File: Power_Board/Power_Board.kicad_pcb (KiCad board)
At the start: 2 copper layers, 3 parts, among them J1 Conn_01x10, J2 Conn_01x10, J3 Conn_01x10_Female

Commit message: few things added
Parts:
- removed J2: Conn_01x10, Connector_PinHeader_2.00mm:PinHeader_1x10_P2.00mm_Vertical
- removed J3: Conn_01x10_Female, Connector_PinSocket_1.00mm:PinSocket_1x10_P1.00mm_Vertical
- added J1_left1: Conn_01x12_Female, Connector_PinSocket_2.54mm:PinSocket_1x12_P2.54mm_Vertical, F.Cu at (187.9, 65.2)
- added J1_right1: Conn_01x12_Female, Connector_PinSocket_2.54mm:PinSocket_1x12_P2.54mm_Vertical, F.Cu at (172.7, 65.2)
- added R1: R, Resistor_SMD:R_0201_0603Metric, F.Cu at (157.8, 60.0)
- J1: value Conn_01x10 -> Screw_Terminal_01x02; footprint Connector_PinHeader_2.00mm:PinHeader_1x10_P2.00mm_Vertical -> TerminalBlock_RND:TerminalBlock_RND_205-00001_1x02_P5.00mm_Horizontal
- moved J1 52.4 mm to (199.6, 54.8)
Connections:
- J1 pad 1: unconnected-(J1-Pad1) -> GND
- J1 pad 2: unconnected-(J1-Pad2) -> +BATT
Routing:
- net VBUS: track 0.00 -> 19.4 mm
- net unconnected-(J1_right1-Pad2): track 0.00 -> 17.9 mm

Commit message: LED added for git test
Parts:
- added D1: LED, LED_THT:LED_D5.0mm, F.Cu at (213.4, 66.0)
- added D2: LED, LED_THT:LED_D5.0mm, F.Cu at (213.4, 76.2)
- added R1: R, OptoDevice:R_LDR_5.2x5.2mm_P3.5mm_Horizontal, F.Cu at (220.0, 66.0)
- added R2: R, OptoDevice:R_LDR_5.2x5.2mm_P3.5mm_Horizontal, F.Cu at (220.0, 76.2)

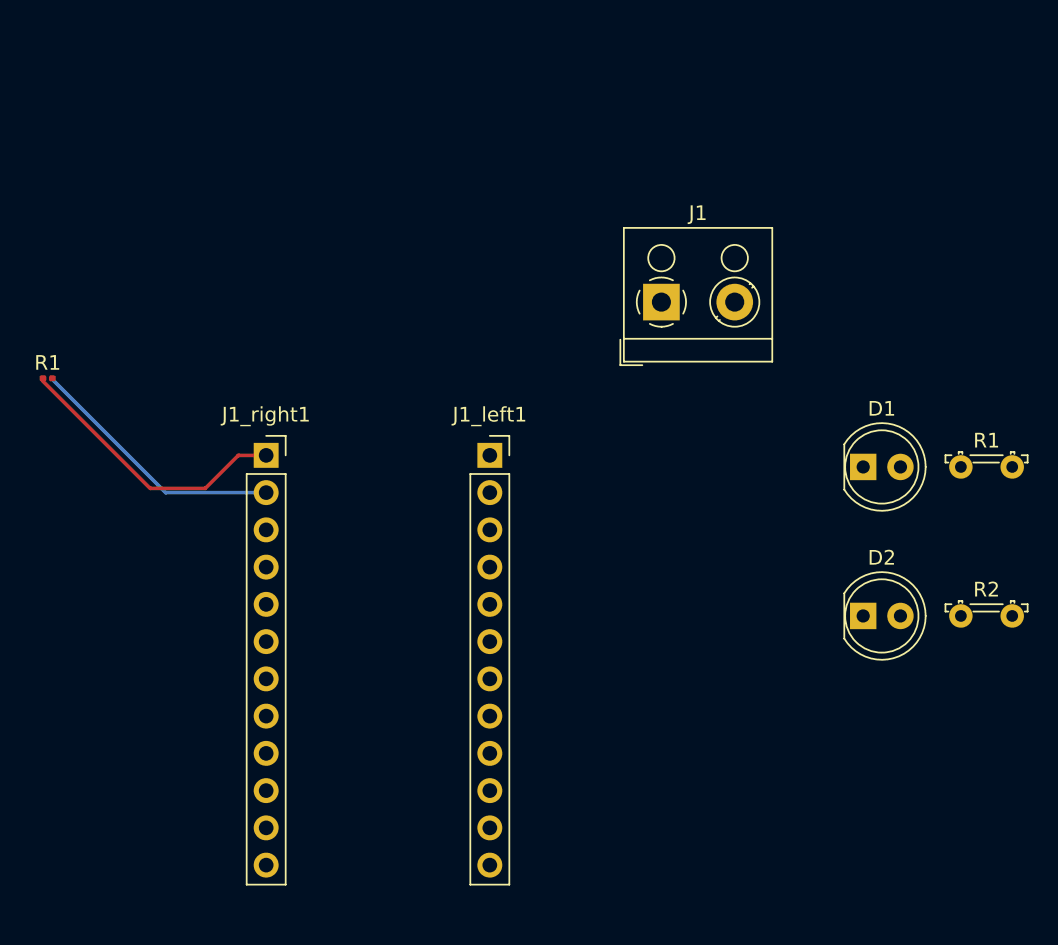
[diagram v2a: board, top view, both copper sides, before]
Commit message: sensor adeed
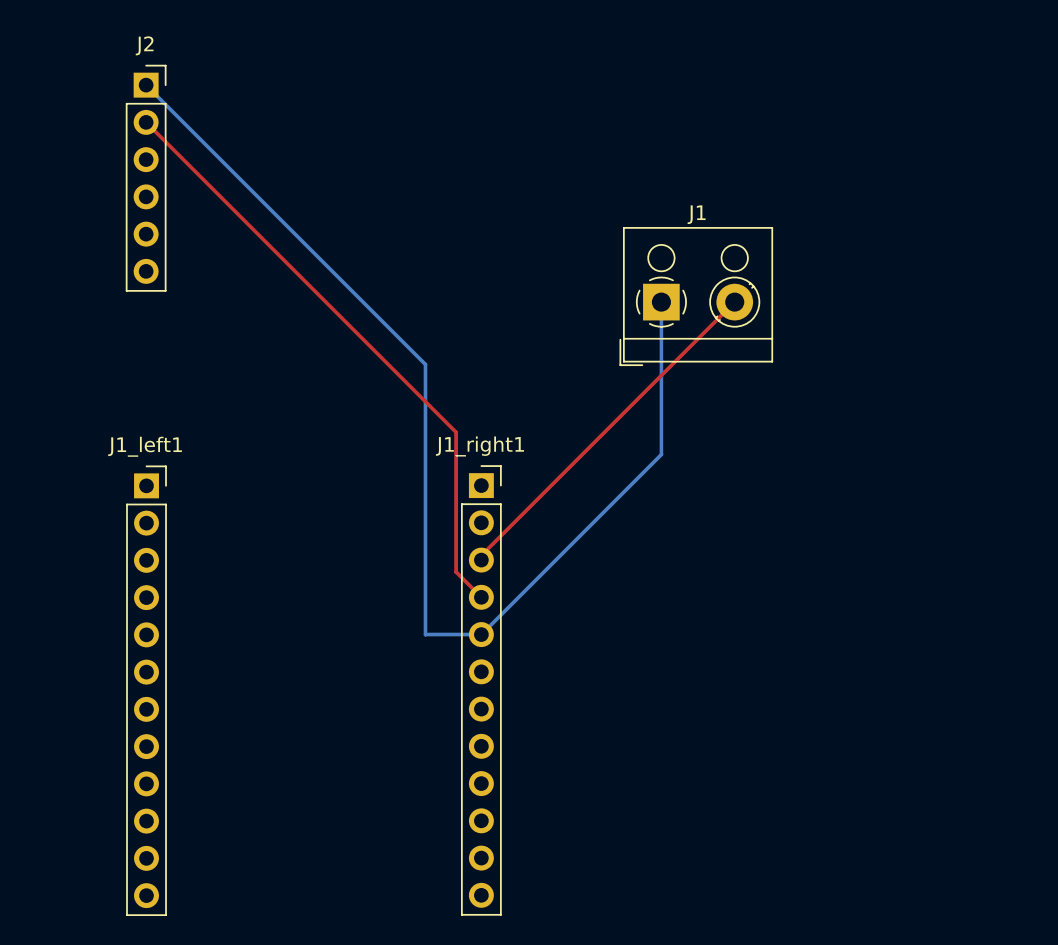
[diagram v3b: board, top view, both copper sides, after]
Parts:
- removed D1, D2: LED, LED_THT:LED_D5.0mm
- removed R1: R, Resistor_SMD:R_0201_0603Metric
- removed R1, R2: R, OptoDevice:R_LDR_5.2x5.2mm_P3.5mm_Horizontal
- added J2: Conn_01x06_Female, Connector_PinSocket_2.54mm:PinSocket_1x06_P2.54mm_Vertical, F.Cu at (164.5, 40.0)
- moved J1_left1 23.5 mm to (164.5, 67.3)
- moved J1_right1 14.8 mm to (187.3, 67.3)
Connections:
- J1 pad 2: +BATT -> VBUS
- J1_right1 pad 4: VDDOUT -> 3V3
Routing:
- net GND: track 0.00 -> 76.9 mm
- net 3V3: track 0.00 -> 41.9 mm
- net unconnected-(J1_right1-Pad2): track 17.9 -> 0.00 mm
- net VBUS: track 19.4 -> 24.7 mm

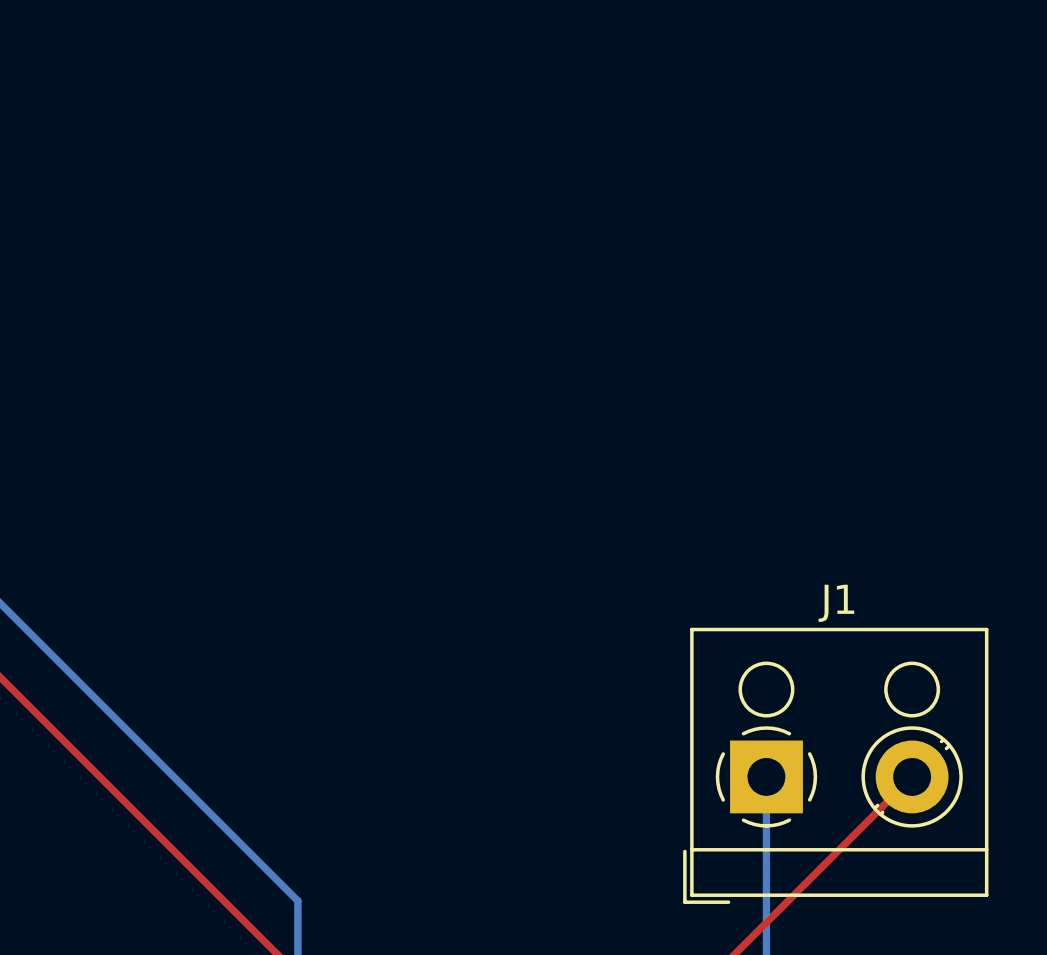
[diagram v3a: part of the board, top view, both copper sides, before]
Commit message: rectifier added
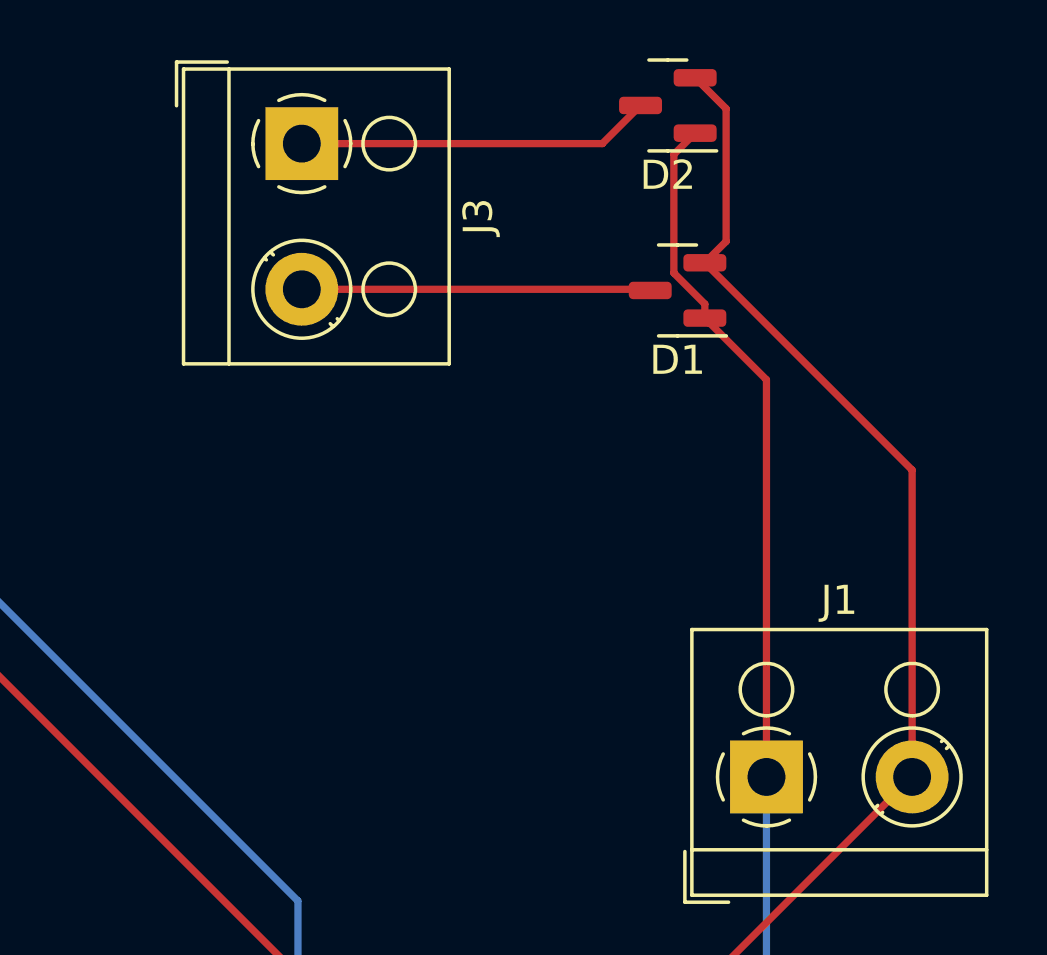
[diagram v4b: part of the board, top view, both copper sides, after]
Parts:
- added D1: BAT54S, Package_TO_SOT_SMD:SOT-23, F.Cu at (196.5, 38.1)
- added D2: BAT54S, Package_TO_SOT_SMD:SOT-23, F.Cu at (196.2, 31.8)
- added J3: Screw_Terminal_01x02, TerminalBlock_RND:TerminalBlock_RND_205-00001_1x02_P5.00mm_Horizontal, F.Cu at (183.7, 33.1)
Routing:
- net VBUS: track 24.7 -> 52.4 mm
- net GND: track 76.9 -> 100.6 mm
- net Net-(D2-Pad3): track 0.00 -> 12.2 mm
- net Net-(D1-Pad3): track 0.00 -> 12.0 mm

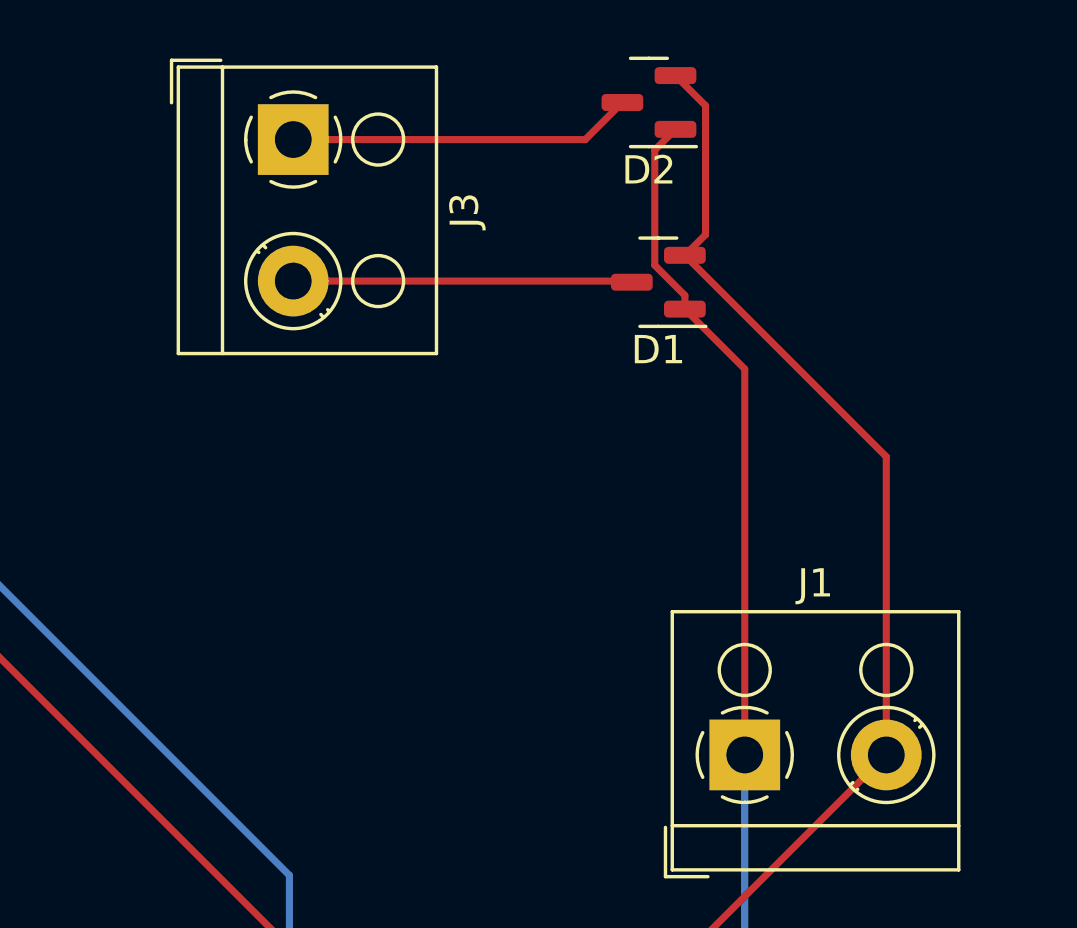
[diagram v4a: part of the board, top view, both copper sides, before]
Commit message: Changed diod footprint
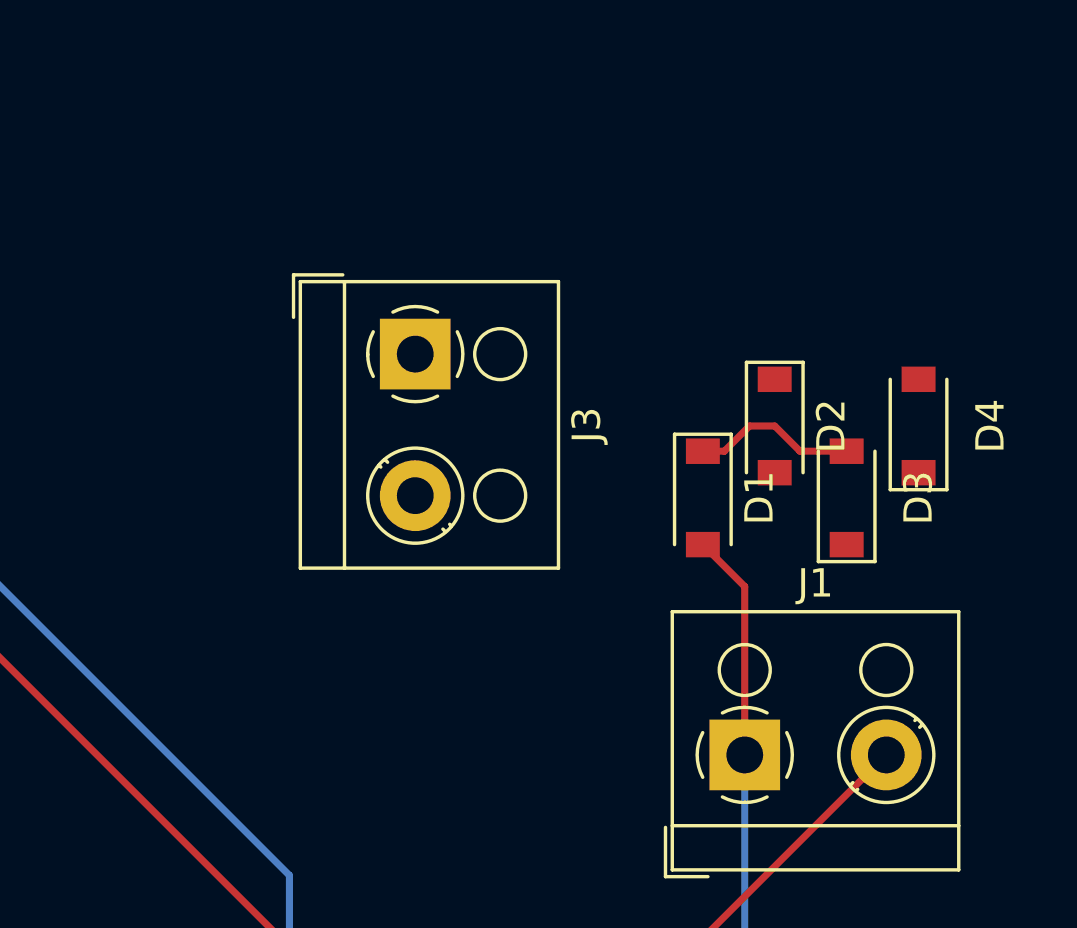
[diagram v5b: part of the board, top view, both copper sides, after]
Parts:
- added D3: 1N4148W, Diode_SMD:D_SOD-123, F.Cu at (203.2, 45.7)
- added D4: 1N4148W, Diode_SMD:D_SOD-123, F.Cu at (205.7, 43.2)
- D1, D2: value BAT54S -> 1N4148W; footprint Package_TO_SOT_SMD:SOT-23 -> Diode_SMD:D_SOD-123
- moved D2 12.3 mm to (200.7, 43.2), turned to -90 degrees
- moved J3 8.72 mm to (188.0, 40.6)
- moved D1 7.78 mm to (198.1, 45.7), turned to -90 degrees
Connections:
- D1 pad 1: GND -> Net-(J3-Pad2)
- D1 pad 2: VBUS -> GND
- D2 pad 1: GND -> Net-(J3-Pad1)
- D2 pad 2: VBUS -> GND
- J3 pad 1: Net-(D2-Pad3) -> Net-(J3-Pad1)
- J3 pad 2: Net-(D1-Pad3) -> Net-(J3-Pad2)
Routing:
- net VBUS: track 52.4 -> 24.7 mm
- net GND: track 100.6 -> 85.0 mm
- net Net-(D2-Pad3): track 12.2 -> 0.00 mm
- net Net-(D1-Pad3): track 12.0 -> 0.00 mm
- net Net-(J3-Pad2): track 0.00 -> 5.82 mm

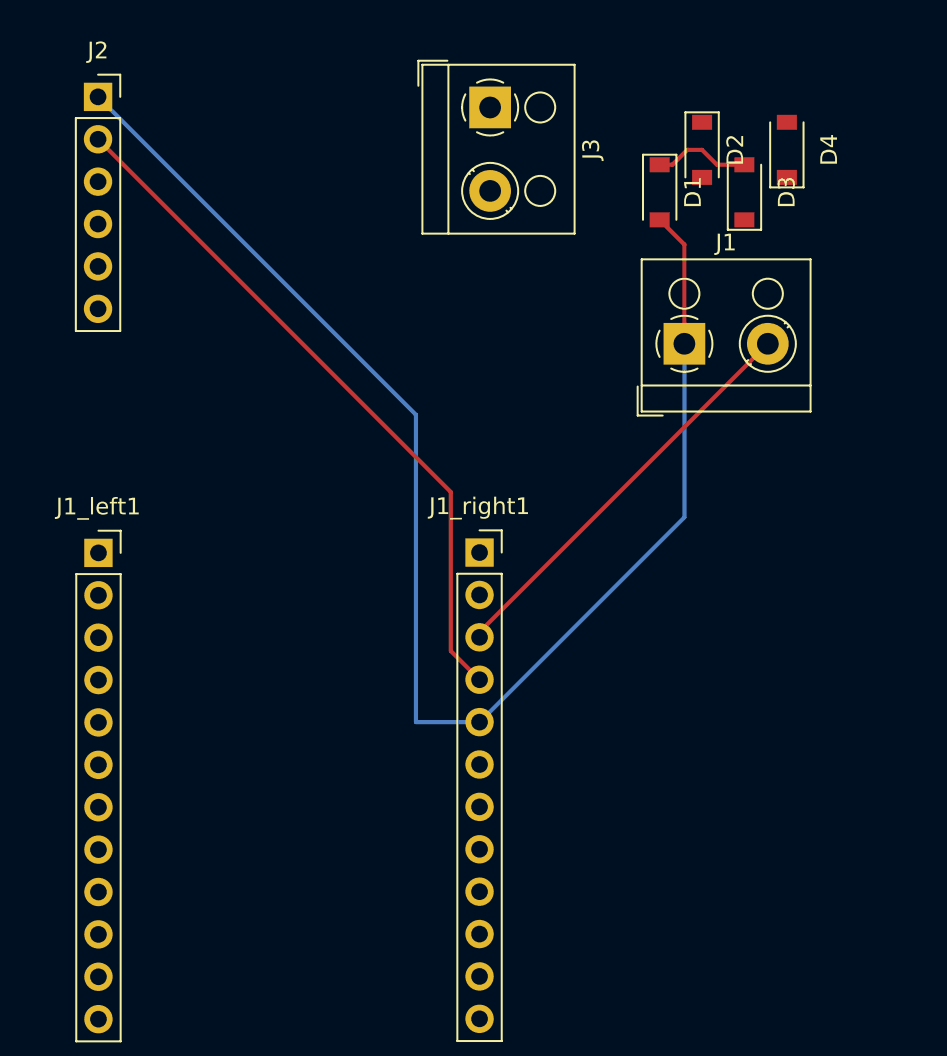
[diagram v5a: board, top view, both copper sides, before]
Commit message: voltage regulator added
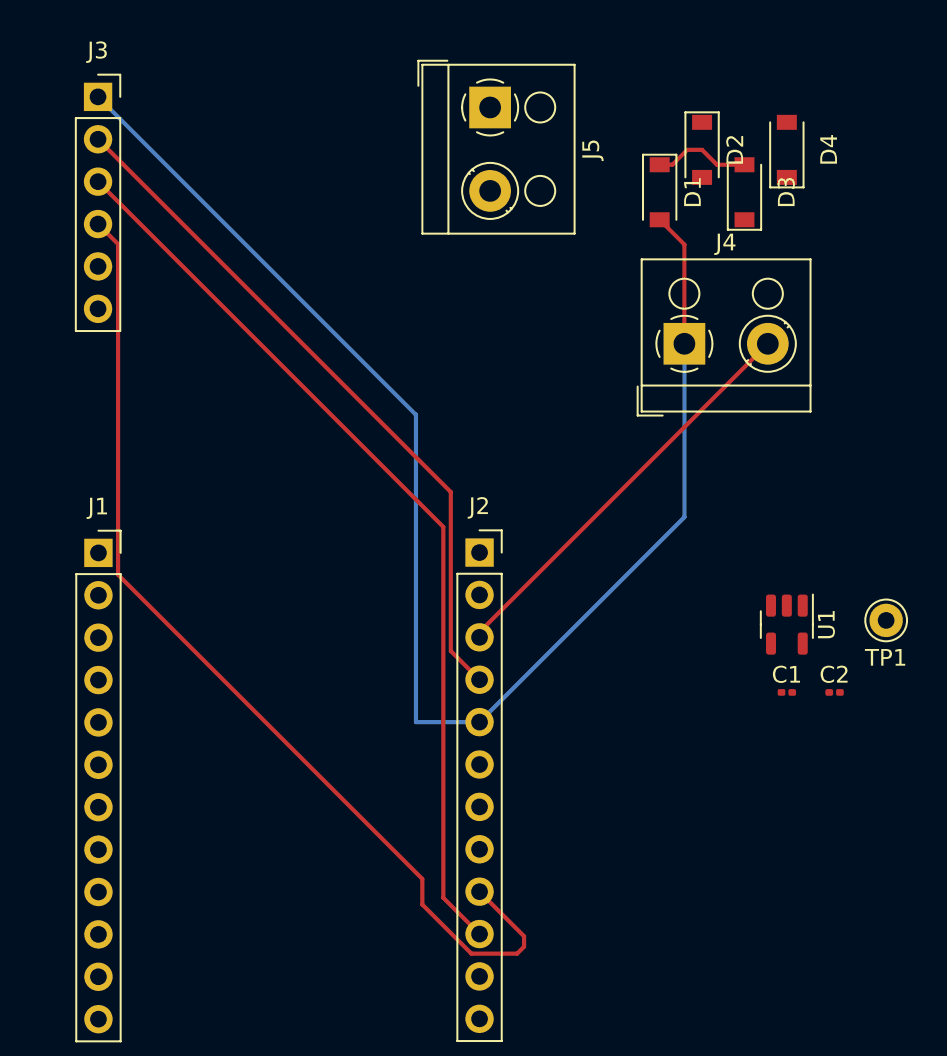
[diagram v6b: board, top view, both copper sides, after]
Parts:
- added C1: 1uF, Capacitor_SMD:C_0201_0603Metric, F.Cu at (205.7, 75.7)
- added C2: 1uF, Capacitor_SMD:C_0201_0603Metric, F.Cu at (208.6, 75.7)
- added TP1: TestPoint, Connector_Pin:Pin_D1.0mm_L10.0mm, F.Cu at (211.7, 71.4)
- added U1: TLV73333PDBV, Package_TO_SOT_SMD:SOT-23-5, F.Cu at (205.7, 71.6)
- renumbered J1_left1 to J1, J1_right1 to J2, J2 to J3, J1 to J4, J3 to J5
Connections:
- J2 pad 4: 3V3 -> VDDOUT
- J3 pad 3: SDA -> 1.13
- J3 pad 4: SCL -> 1.15
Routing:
- net 1.15: track 0.00 -> 60.7 mm
- net 1.13: track 0.00 -> 54.6 mm
- net VDDOUT: track 0.00 -> 41.9 mm
- net 3V3: track 41.9 -> 0.00 mm

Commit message: latest update with rectifier
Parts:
- removed C1, C2: 1uF, Capacitor_SMD:C_0201_0603Metric
- removed D3, D4: 1N4148W, Diode_SMD:D_SOD-123
- removed U1: TLV73333PDBV, Package_TO_SOT_SMD:SOT-23-5
- added TP2: VEH_2, Connector_Pin:Pin_D1.0mm_L10.0mm, F.Cu at (171.2, 80.7)
- added TP3: VEH_OUT, Connector_Pin:Pin_D1.0mm_L10.0mm, F.Cu at (181.2, 68.8)
- D1, D2: value 1N4148W -> BAT54S; footprint Diode_SMD:D_SOD-123 -> Package_TO_SOT_SMD:SOT-23
- J1, J2: value Conn_01x12_Female -> Conn_01x10_Female; footprint Connector_PinSocket_2.54mm:PinSocket_1x12_P2.54mm_Vertical -> Connector_PinSocket_2.54mm:PinSocket_1x10_P2.54mm_Vertical
- TP1: value TestPoint -> VEH_1
- moved TP1 45.5 mm to (167.1, 80.7)
- moved D2 36.5 mm to (176.8, 70.8), turned to 0 degrees
- moved D1 25.2 mm to (181.4, 64.5), turned to 0 degrees
- moved J2 24.2 mm to (167.4, 53.6)
- moved J3 18.2 mm to (176.6, 53.6)
- moved J5 17.5 mm to (182.4, 57.3), turned to 0 degrees
- moved J1 15.7 mm to (172.0, 53.6)
- moved J4 5.68 mm to (194.5, 57.3)
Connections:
- D1 pad 1: Net-(D1-Pad1) -> GND
- D1 pad 2: GND -> VBUS
- D2 pad 1: Net-(D2-Pad1) -> (no net)
- D2 pad 2: GND -> (no net)
- J1 pad 1: unconnected-(J1-Pad1) -> 0.13
- J1 pad 10: 0.09 -> GND
- J1 pad 2: unconnected-(J1-Pad2) -> 0.15
- J1 pad 3: 0.13 -> 0.17
- J1 pad 4: 0.15 -> 0.20
- J1 pad 5: 0.17 -> 0.22
- J1 pad 6: 0.20 -> 0.24
- J1 pad 7: 0.22 -> 1.00
- J1 pad 8: 0.24 -> 0.09
- J1 pad 9: 1.00 -> 0.10
- J2 pad 1: unconnected-(J2-Pad1) -> VBUS
- J2 pad 10: 1.13 -> GND
- J2 pad 2: unconnected-(J2-Pad2) -> VDDOUT
- J2 pad 3: VBUS -> GND
- J2 pad 4: VDDOUT -> 0.31
- J2 pad 5: GND -> 0.29
- J2 pad 6: 0.31 -> 0.02
- J2 pad 7: 0.29 -> 1.15
- J2 pad 8: 0.02 -> 1.13
- J2 pad 9: 1.15 -> 1.10
- J3 pad 2: 3V3 -> VDDOUT
- J3 pad 3: 1.13 -> 1.15
- J3 pad 4: 1.15 -> 1.13
- J5 pad 1: Net-(D2-Pad1) -> Net-(D2-Pad3)
- J5 pad 2: Net-(D1-Pad1) -> Net-(D1-Pad3)
- TP1 pad 1: unconnected-(TP1-Pad1) -> Net-(D1-Pad3)
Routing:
- net GND: track 85.0 -> 0.00 mm
- net 1.15: track 60.7 -> 0.00 mm
- net 1.13: track 54.6 -> 0.00 mm
- net VDDOUT: track 41.9 -> 0.00 mm
- net VBUS: track 24.7 -> 0.00 mm
- net Net-(D1-Pad1): track 5.82 -> 0.00 mm
